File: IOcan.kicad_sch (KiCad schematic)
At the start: 0 parts

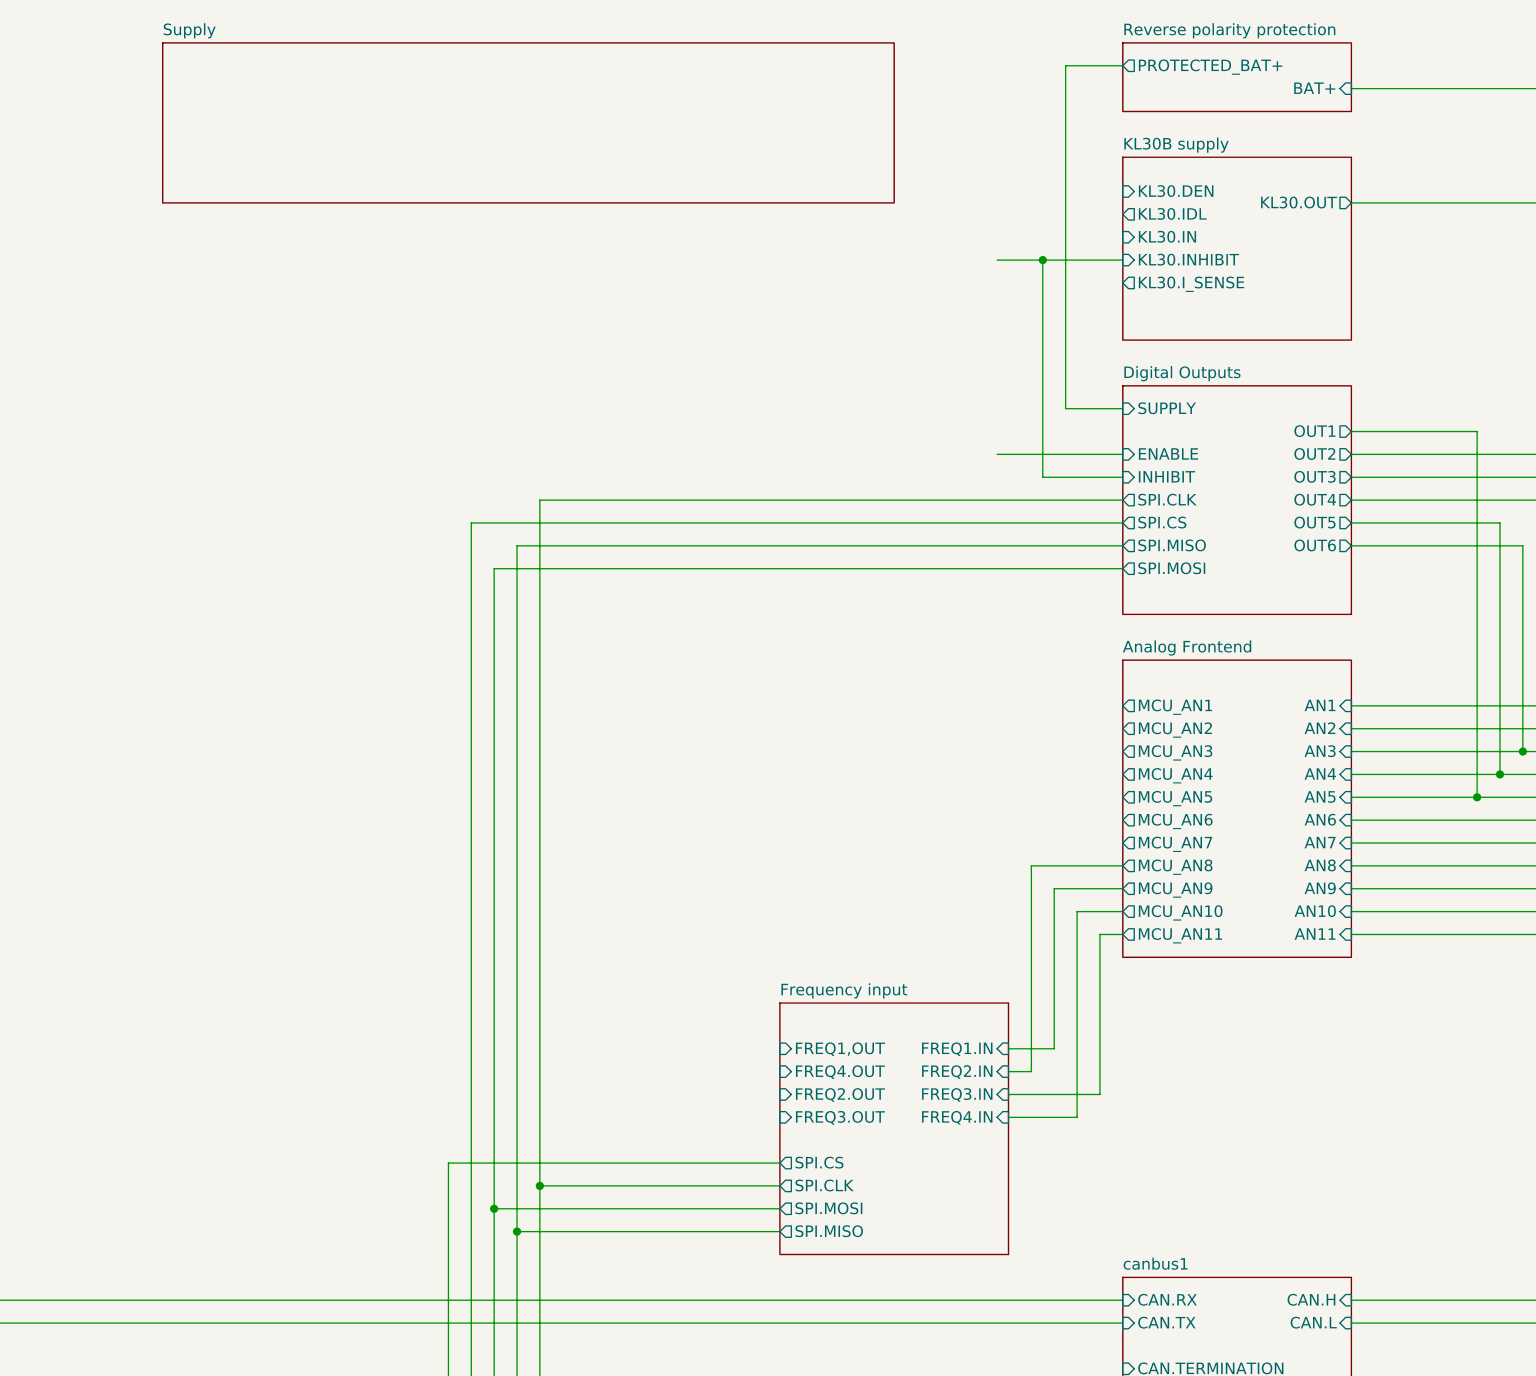
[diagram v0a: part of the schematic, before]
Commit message: Finished schematic of the FreqIn channels
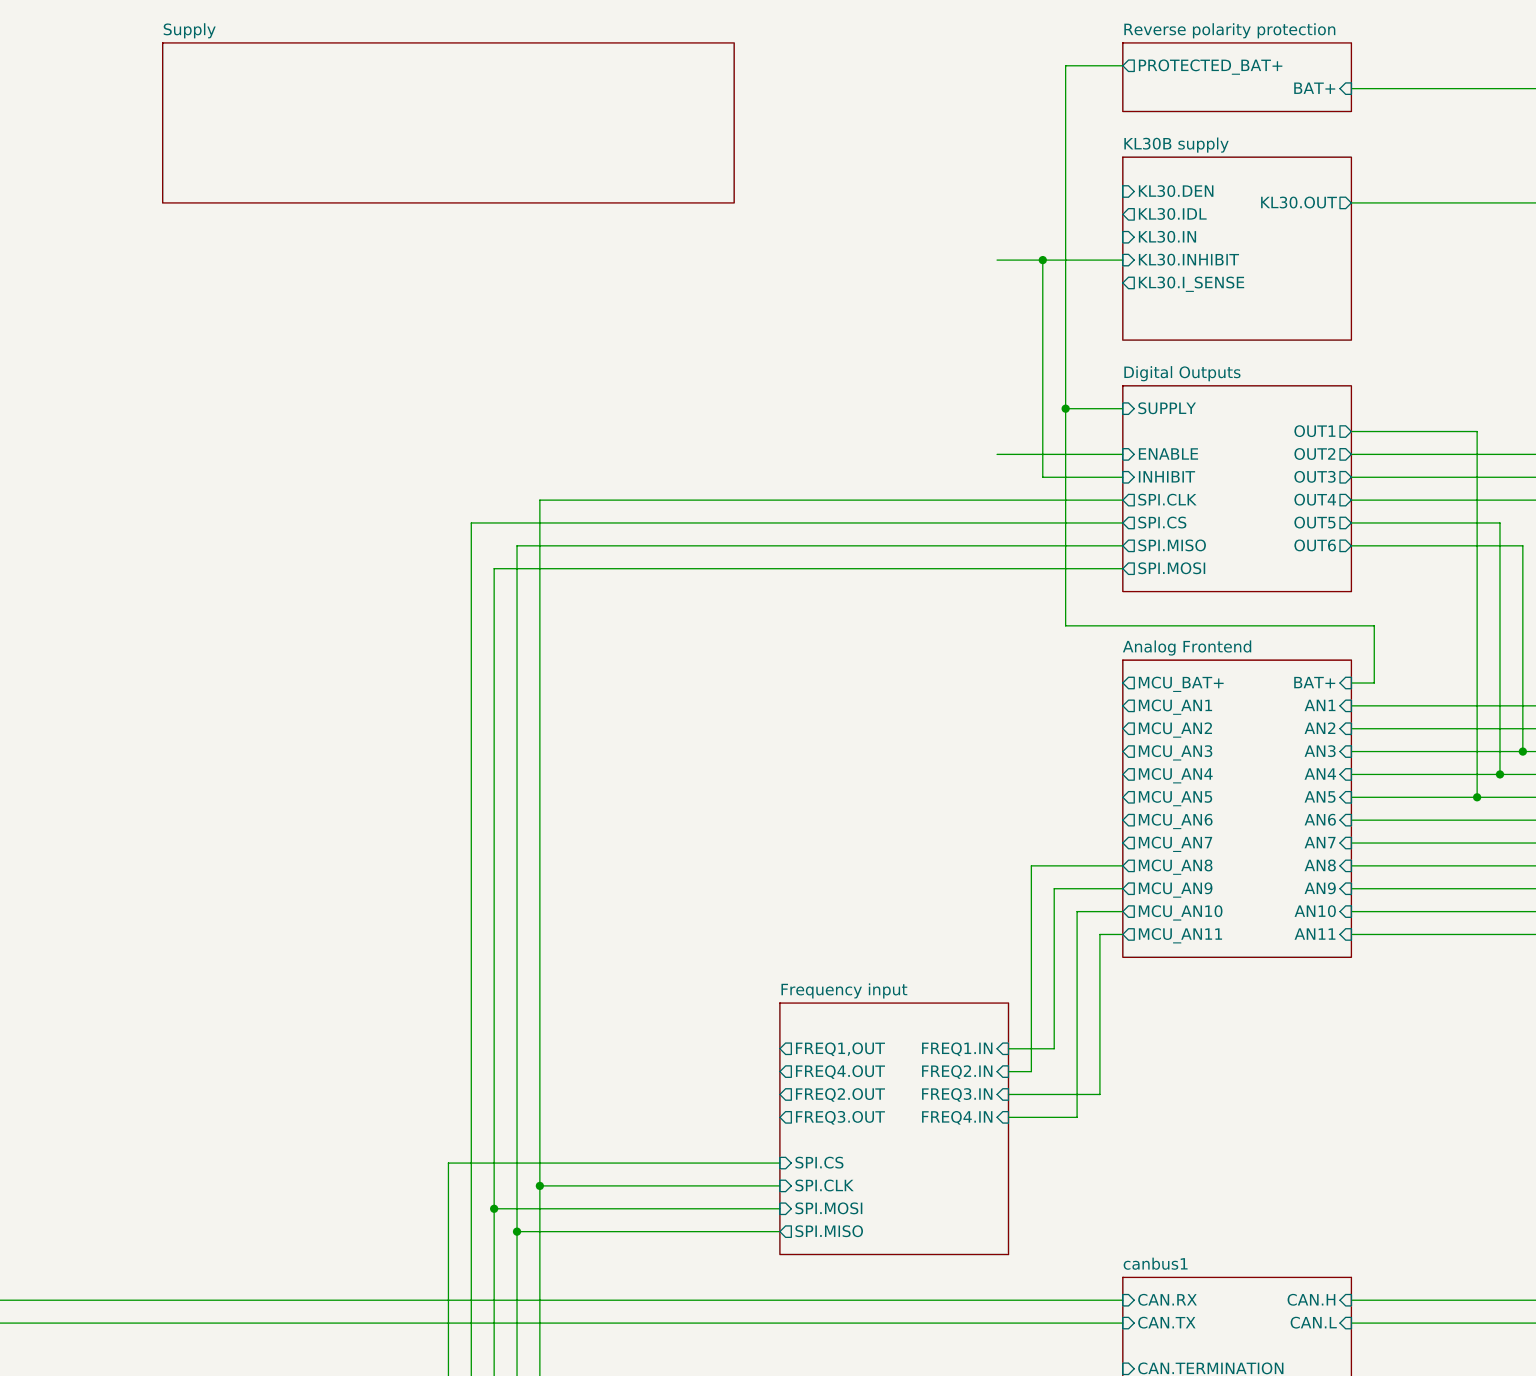
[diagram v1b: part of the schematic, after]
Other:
- sheet Analog Frontend ports: added BAT+, MCU_BAT+; removed none

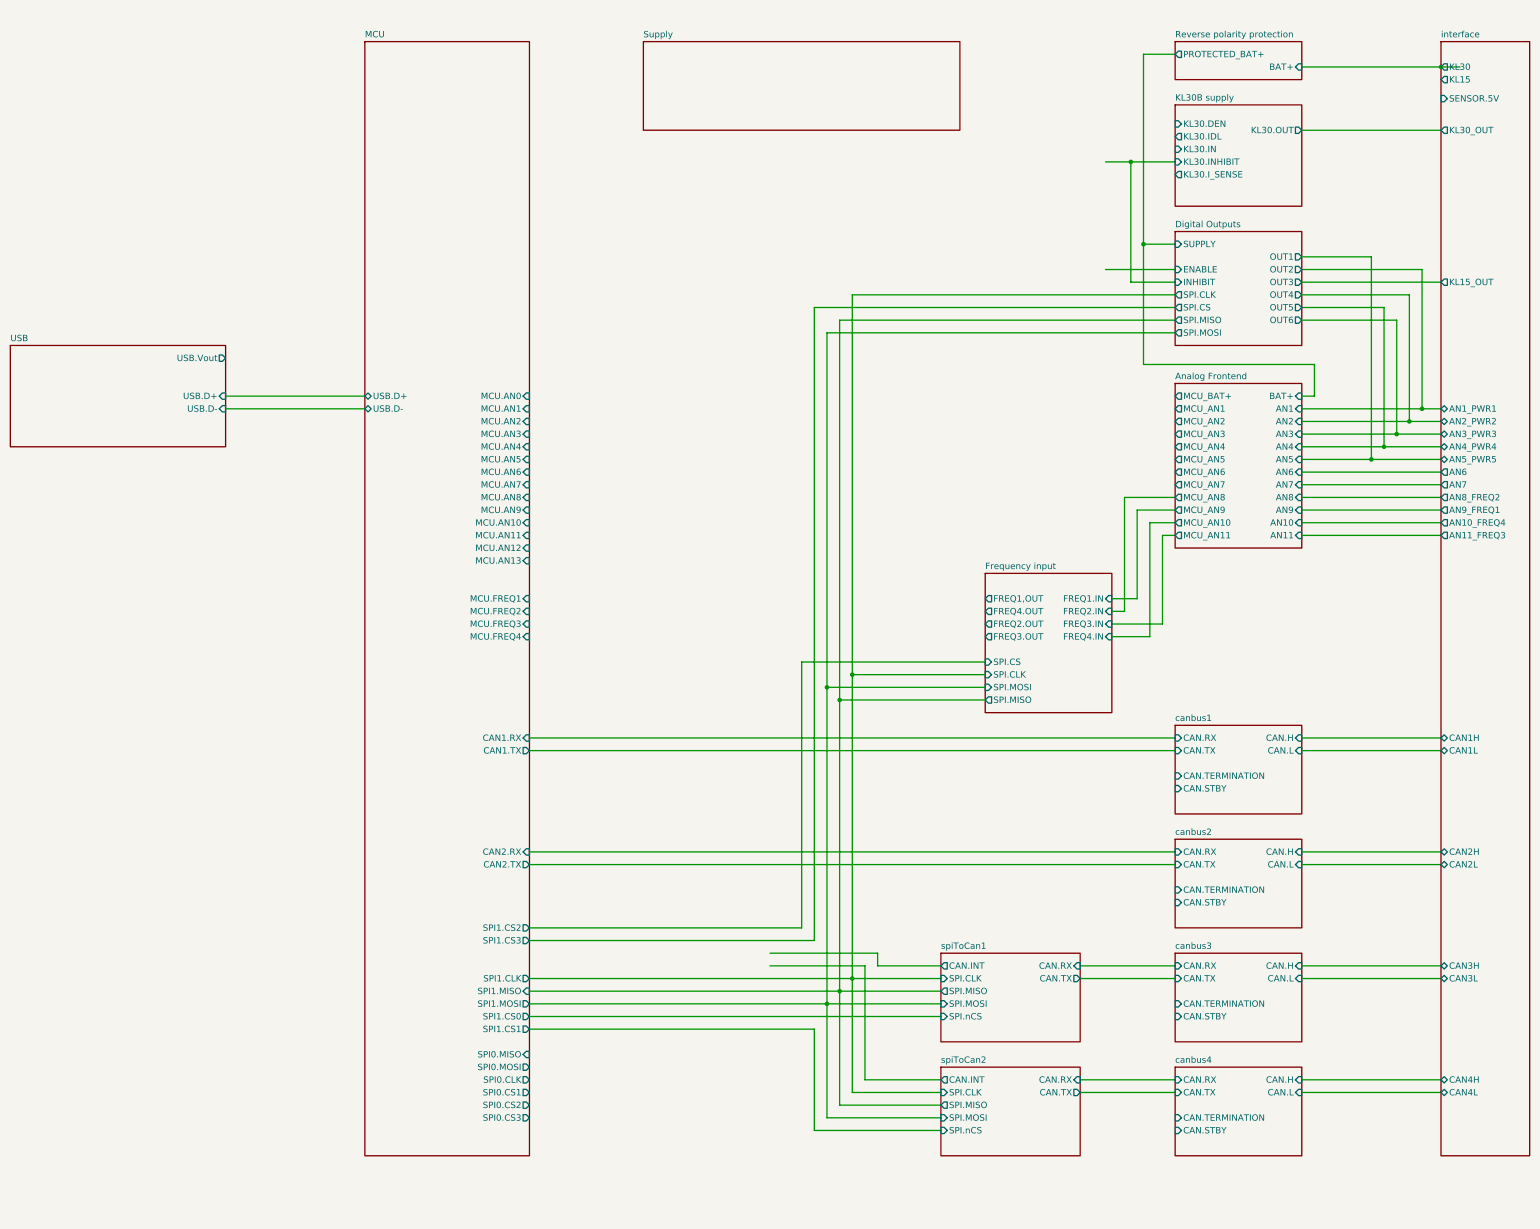
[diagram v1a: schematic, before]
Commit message: Added Wakeup, supply, more pins on MCU
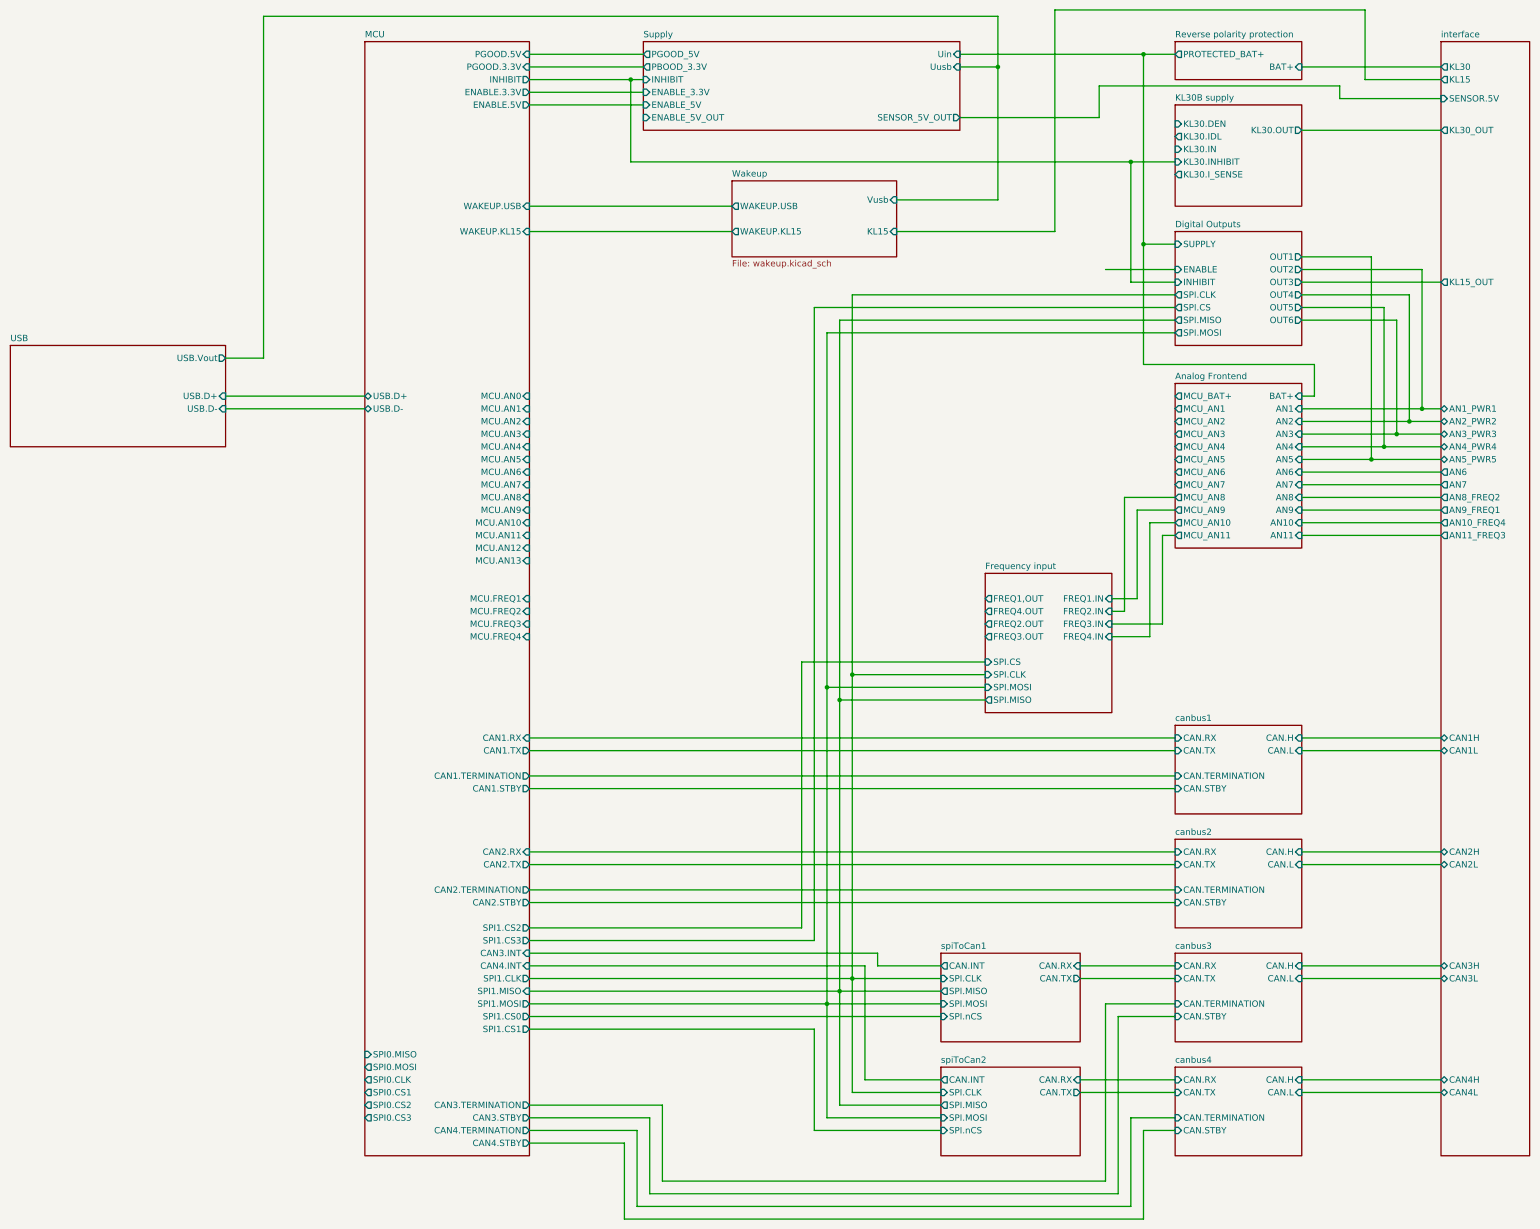
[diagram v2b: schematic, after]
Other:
- added sheet Wakeup (wakeup.kicad_sch)
- sheet MCU ports: added CAN1.STBY, CAN1.TERMINATION, CAN2.STBY, CAN2.TERMINATION, CAN3.INT, CAN3.STBY, CAN3.TERMINATION, CAN4.INT, CAN4.STBY, CAN4.TERMINATION, ENABLE.3.3V, ENABLE.5V, INHIBIT, PGOOD.3.3V, PGOOD.5V, WAKEUP.KL15, WAKEUP.USB; removed none
- sheet Supply ports: added ENABLE_3.3V, ENABLE_5V, ENABLE_5V_OUT, INHIBIT, PBOOD_3.3V, PGOOD_5V, SENSOR_5V_OUT, Uin, Uusb; removed none

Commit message: Added routing for Freq Inputs
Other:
- sheet MCU ports: added MCU.FREQ0, MCU.FREQ5; removed none
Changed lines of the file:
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@@
 	)
 	(junction
-		(at 229.87 154.94)
+		(at 344.17 99.06)
 		(diameter 0)
 		(color 0 0 0 0)
 	)
 	(junction
-		(at 344.17 99.06)
+		(at 229.87 213.36)
 		(diameter 0)
 		(color 0 0 0 0)
 	)
 	(junction
-		(at 229.87 213.36)
+		(at 232.41 149.86)
 		(diameter 0)
 		(color 0 0 0 0)
 	)
 	(junction
-		(at 290.83 63.5)
+		(at 229.87 154.94)
 		(diameter 0)
 		(color 0 0 0 0)
 	)
 	(junction
-		(at 339.09 104.14)
+		(at 290.83 63.5)
 		(diameter 0)
 		(color 0 0 0 0)
 	)
 	(junction
-		(at 187.96 30.48)
+		(at 339.09 104.14)
 		(diameter 0)
 		(color 0 0 0 0)
 	)
 	(junction
-		(at 227.33 152.4)
+		(at 187.96 30.48)
 		(diameter 0)
 		(color 0 0 0 0)
@@
 	)
 	(junction
-		(at 232.41 149.86)
+		(at 336.55 106.68)
 		(diameter 0)
 		(color 0 0 0 0)
 	)
 	(junction
-		(at 336.55 106.68)
+		(at 227.33 152.4)
 		(diameter 0)
 		(color 0 0 0 0)
@@
 	(wire
 		(pts
+			(xy 176.53 134.62) (xy 167.64 134.62)
+		)
+		(stroke
+			(width 0)
+			(type default)
+		)
+	)
+	(wire
+		(pts
 			(xy 285.75 254) (xy 285.75 218.44)
 		)
@@
 	(wire
 		(pts
+			(xy 259.08 137.16) (xy 176.53 137.16)
+		)
+		(stroke
+			(width 0)
+			(type default)
+		)
+	)
+	(wire
+		(pts
 			(xy 273.05 16.51) (xy 335.28 16.51)
 		)
@@
 	(wire
 		(pts
+			(xy 179.07 144.78) (xy 179.07 134.62)
+		)
+		(stroke
+			(width 0)
+			(type default)
+		)
+	)
+	(wire
+		(pts
 			(xy 237.49 205.74) (xy 237.49 208.28)
 		)
@@
 	(wire
 		(pts
+			(xy 181.61 142.24) (xy 167.64 142.24)
+		)
+		(stroke
+			(width 0)
+			(type default)
+		)
+	)
+	(wire
+		(pts
 			(xy 227.33 152.4) (xy 259.08 152.4)
 		)
@@
 	(wire
 		(pts
+			(xy 176.53 137.16) (xy 176.53 134.62)
+		)
+		(stroke
+			(width 0)
+			(type default)
+		)
+	)
+	(wire
+		(pts
 			(xy 167.64 185.42) (xy 297.18 185.42)
 		)
@@
 	(wire
 		(pts
+			(xy 181.61 139.7) (xy 181.61 142.24)
+		)
+		(stroke
+			(width 0)
+			(type default)
+		)
+	)
+	(wire
+		(pts
 			(xy 330.2 34.29) (xy 350.52 34.29)
 		)
@@
 	(wire
 		(pts
+			(xy 259.08 142.24) (xy 200.66 142.24)
+		)
+		(stroke
+			(width 0)
+			(type default)
+		)
+	)
+	(wire
+		(pts
 			(xy 187.96 46.99) (xy 288.29 46.99)
 		)
@@
 	(wire
 		(pts
+			(xy 173.99 140.97) (xy 173.99 139.7)
+		)
+		(stroke
+			(width 0)
+			(type default)
+		)
+	)
+	(wire
+		(pts
 			(xy 167.64 208.28) (xy 234.95 208.28)
 		)
@@
 	(wire
 		(pts
+			(xy 179.07 134.62) (xy 259.08 134.62)
+		)
+		(stroke
+			(width 0)
+			(type default)
+		)
+	)
+	(wire
+		(pts
 			(xy 232.41 149.86) (xy 232.41 210.82)
 		)
@@
 	(wire
 		(pts
+			(xy 200.66 142.24) (xy 200.66 140.97)
+		)
+		(stroke
+			(width 0)
+			(type default)
+		)
+	)
+	(wire
+		(pts
 			(xy 322.58 104.14) (xy 339.09 104.14)
 		)
@@
 	(wire
 		(pts
+			(xy 173.99 139.7) (xy 167.64 139.7)
+		)
+		(stroke
+			(width 0)
+			(type default)
+		)
+	)
+	(wire
+		(pts
 			(xy 283.21 68.58) (xy 297.18 68.58)
 		)
@@
 	(wire
 		(pts
+			(xy 200.66 140.97) (xy 173.99 140.97)
+		)
+		(stroke
+			(width 0)
+			(type default)
+		)
+	)
+	(wire
+		(pts
 			(xy 234.95 231.14) (xy 234.95 208.28)
 		)
@@
 	(wire
 		(pts
+			(xy 259.08 139.7) (xy 181.61 139.7)
+		)
+		(stroke
+			(width 0)
+			(type default)
+		)
+	)
+	(wire
+		(pts
 			(xy 114.3 17.78) (xy 114.3 86.36)
 		)
@@
 	(wire
 		(pts
+			(xy 167.64 144.78) (xy 179.07 144.78)
+		)
+		(stroke
+			(width 0)
+			(type default)
+		)
+	)
+	(wire
+		(pts
 			(xy 167.64 162.56) (xy 297.18 162.56)
 		)
@@
 		)
 		(pin "FREQ2.OUT" output
-			(at 259.08 139.7 180)
+			(at 259.08 137.16 180)
 			(effects
 				(font
@@
 		)
 		(pin "FREQ3.OUT" output
-			(at 259.08 142.24 180)
+			(at 259.08 139.7 180)
 			(effects
 				(font
@@
 		)
 		(pin "FREQ4.OUT" output
-			(at 259.08 137.16 180)
+			(at 259.08 142.24 180)
 			(effects
 				(font
@@
 			(effects
 				(font
+					(size 1.27 1.27)
+				)
+				(justify right)
+			)
+		)
+		(pin "MCU.FREQ0" input
+			(at 167.64 132.08 0)
+			(effects
+				(font
+					(size 1.27 1.27)
+				)
+				(justify right)
+			)
+		)
+		(pin "MCU.FREQ5" input
+			(at 167.64 144.78 0)
+			(effects
+				(font
